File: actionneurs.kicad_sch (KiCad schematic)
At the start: 89 parts, among them J1 690367280876, J10 ESC_35_1_P, J11 690367280876, J12 ESC_35_2_S, J13 Alim Pompe, J14 690367280876, J16 690367280876, J17 690367280876, J18 690367280876, J19 Alim EV, J20 Alim EV, J21 Alim EV, J22 Alim EV, J23 Alim EV, J24 Alim EV, J25 Alim EV, J26 Alim EV, J27 Alim EV, J28 Alim EV, J29 Alim EV, J30 Alim EV, J6 ESC_35_1_P, J9 ESC_35_1_S, Q1 G2302, Q10 G2302, Q11 G2302, Q12 G2302, Q13 G2302, Q14 G2302, Q15 G2302, Q16 G2302, Q17 G2302, Q18 G2302, Q2 G2302, Q3 G2302, Q4 G2302, Q5 G2302

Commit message: Minor adjust before routing
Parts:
- R10: now fitted; now in the parts list
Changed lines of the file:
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@@
 		(unit 1)
 		(exclude_from_sim no)
-		(in_bom no)
+		(in_bom yes)
 		(on_board yes)
-		(dnp yes)
+		(dnp no)
 		(property "Reference" "R10"
 			(at 238.76 49.53 90)

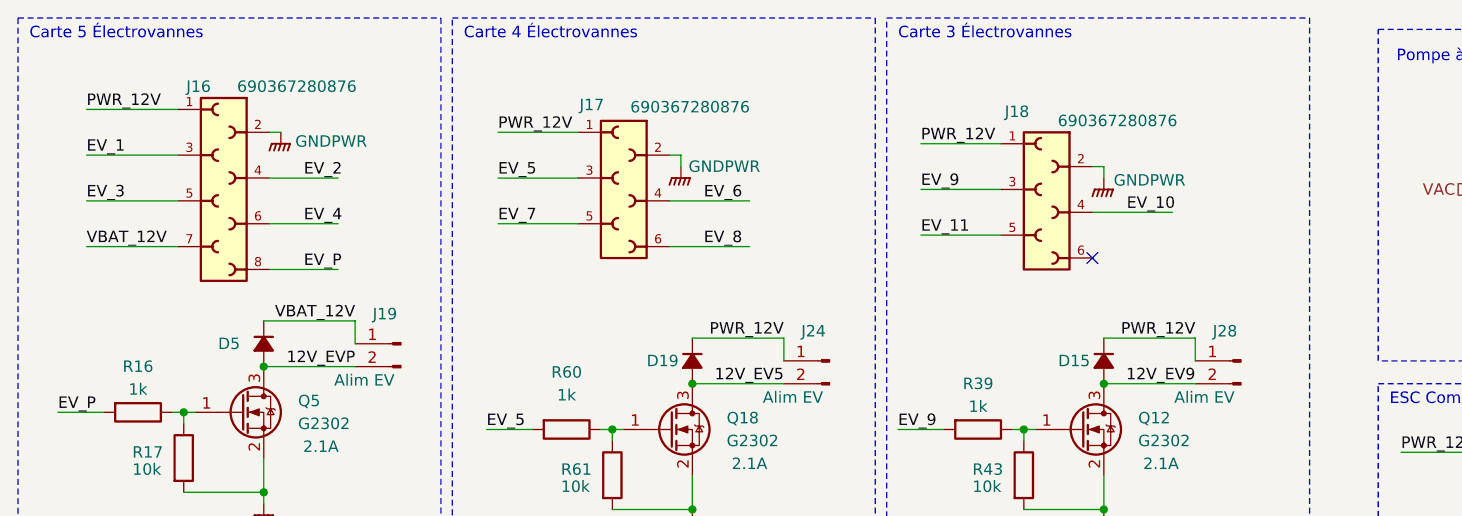
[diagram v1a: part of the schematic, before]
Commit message: ajout capa sur carte peripherique, fin placement serigraphie top
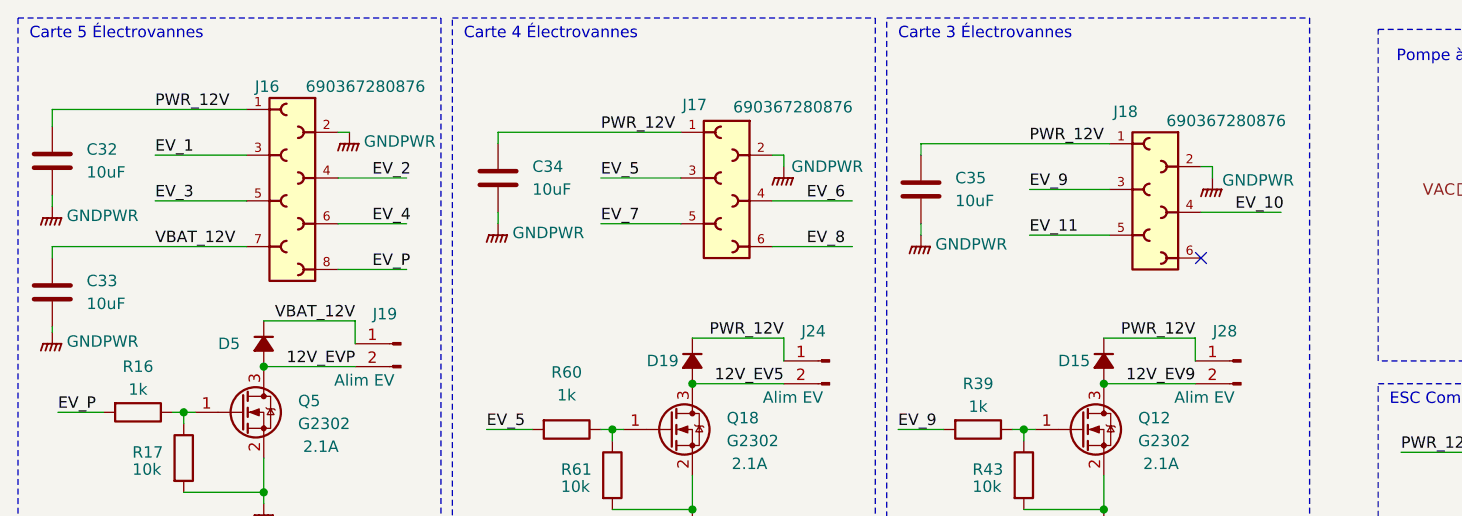
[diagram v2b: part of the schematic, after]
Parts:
- added C32, C33, C34, C35: 10uF, Capacitor_SMD:C_0805_2012Metric, symbol Device:C
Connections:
- net GNDPWR: now also C32.2, C33.2, C34.2, C35.2
- net PWR_12V: now also C32.1, C34.1, C35.1
- net VBAT_12V: now also C33.1
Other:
- moved on the sheet: J16, J17, J18

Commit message: corrrection footprint trim, ajout R64, config JLCPCB ASSY, fin panelisation (TODO: revue et cmd)
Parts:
- D10, D12, D13, D14, D15, D16, D17, D18, D19, D2, D3, D4, D5: value ~ -> 1N4148W
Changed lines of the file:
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@@
 			)
 		)
-		(property "Value" "~"
+		(property "Value" "1N4148W"
 			(at 81.28 142.24 90)
 			(effects
@@
 			)
 		)
-		(property "Value" "~"
+		(property "Value" "1N4148W"
 			(at 191.77 25.4 90)
 			(effects
@@
 			)
 		)
-		(property "Value" "~"
+		(property "Value" "1N4148W"
 			(at 128.27 113.03 90)
 			(effects
@@
 			)
 		)
-		(property "Value" "~"
+		(property "Value" "1N4148W"
 			(at 82.55 80.01 90)
 			(effects
@@
 			)
 		)
-		(property "Value" "~"
+		(property "Value" "1N4148W"
 			(at 82.55 52.07 90)
 			(effects
@@
 			)
 		)
-		(property "Value" "~"
+		(property "Value" "1N4148W"
 			(at 34.925 50.165 90)
 			(effects
@@
 			)
 		)
-		(property "Value" "~"
+		(property "Value" "1N4148W"
 			(at 34.29 168.275 90)
 			(effects
@@
 			)
 		)
-		(property "Value" "~"
+		(property "Value" "1N4148W"
 			(at 34.29 139.065 90)
 			(effects
@@
 			)
 		)
-		(property "Value" "~"
+		(property "Value" "1N4148W"
 			(at 128.27 82.55 90)
 			(effects
@@
 			)
 		)
-		(property "Value" "~"
+		(property "Value" "1N4148W"
 			(at 128.27 52.07 90)
 			(effects
@@
 			)
 		)
-		(property "Value" "~"
+		(property "Value" "1N4148W"
 			(at 35.56 80.01 90)
 			(effects
@@
 			)
 		)
-		(property "Value" "~"
+		(property "Value" "1N4148W"
 			(at 81.28 110.49 90)
 			(effects
@@
 			)
 		)
-		(property "Value" "~"
+		(property "Value" "1N4148W"
 			(at 34.29 109.22 90)
 			(effects
